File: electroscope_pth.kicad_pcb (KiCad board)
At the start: 2 copper layers, 17 parts, among them Q1 Q_PNP_EBC, Q2 Q_NPN_EBC, Q3 Q_PNP_EBC, Q4 Q_NPN_EBC, Q5 Q_PNP_EBC, Q6 Q_NPN_EBC, U1 ANT, U2 ANT

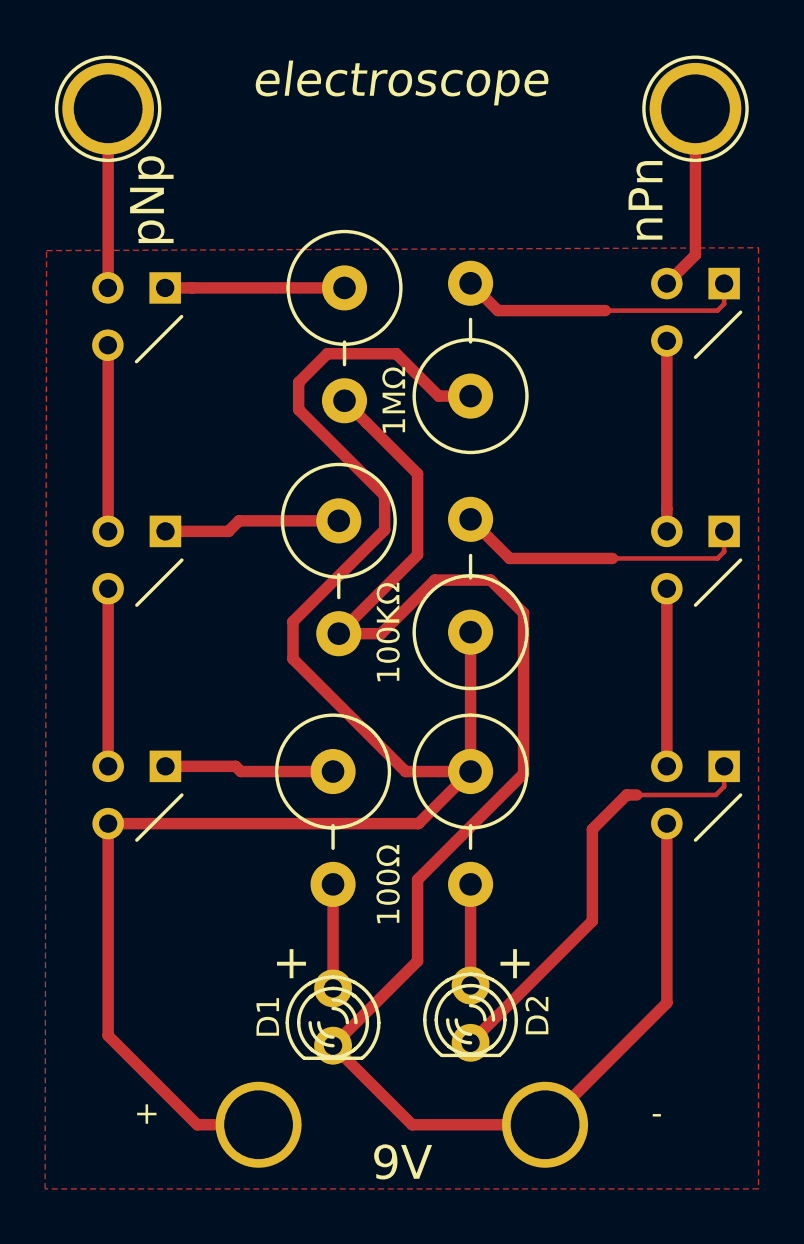
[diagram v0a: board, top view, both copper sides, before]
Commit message: Route to the edges of the board
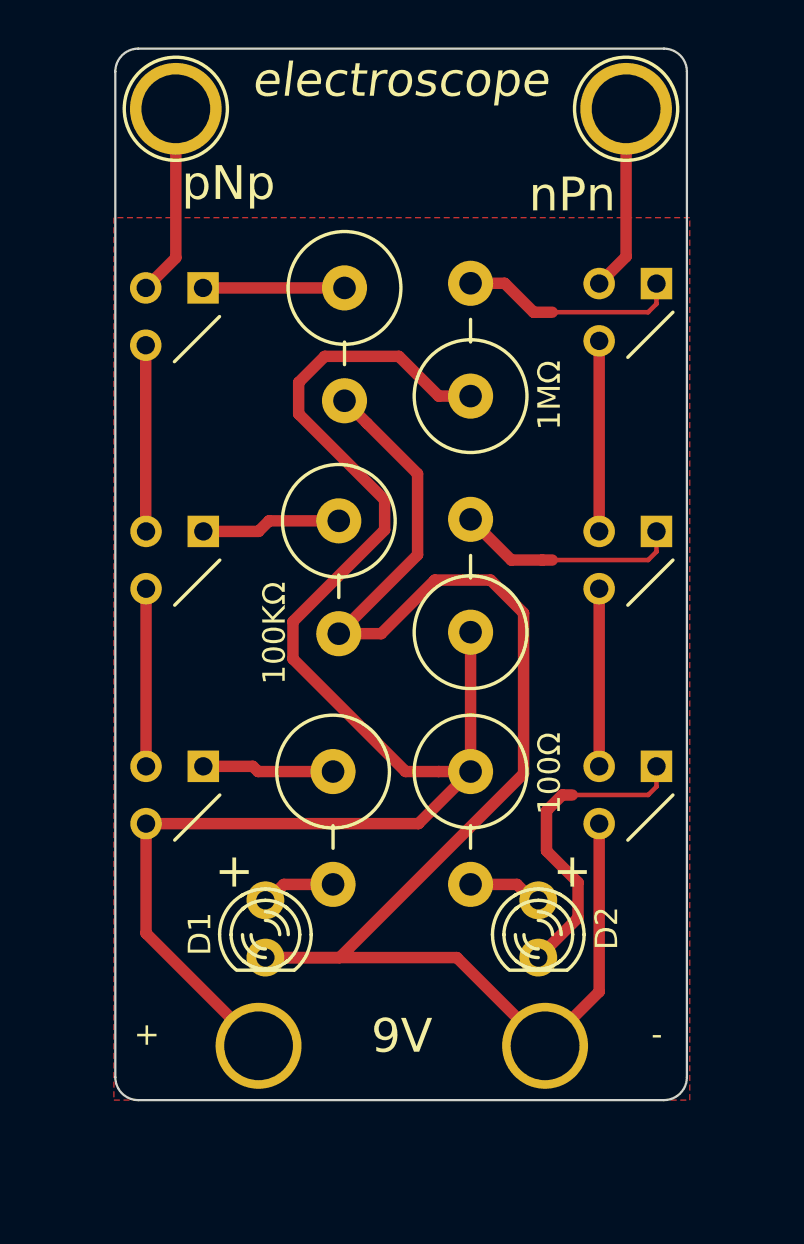
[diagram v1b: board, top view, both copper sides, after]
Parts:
- moved D1 4.92 mm to (133.7, 107.2)
- moved D2 4.82 mm to (145.8, 107.2)
- moved BT1 3.50 mm to (139.8, 112.5)
- moved U1 3.07 mm to (149.7, 70.9)
- moved U2 3.00 mm to (129.7, 70.9)
- moved Q2 3.00 mm to (149.8, 79.9)
- moved Q4 3.00 mm to (149.8, 90.9)
- moved Q6 3.00 mm to (149.8, 101.3)
- moved Q1 1.68 mm to (129.7, 101.3)
- moved Q3 1.68 mm to (129.7, 90.9)
- moved Q5 1.68 mm to (129.7, 80.1)
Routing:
- net VCC: track 75.3 -> 67.7 mm
- net Net-(D2-Pad2): track 19.2 -> 14.0 mm
- net Net-(Q2-Pad3): track 12.8 -> 9.83 mm
- net Net-(Q4-Pad3): track 13.0 -> 10.0 mm
- net GND: track 72.0 -> 69.7 mm
- net Net-(Q3-Pad3): track 7.88 -> 6.20 mm
- net Net-(Q1-Pad3): track 7.52 -> 5.85 mm
- net Net-(Q5-Pad3): track 7.95 -> 6.27 mm
- net Net-(D1-Pad1): track 4.61 -> 3.29 mm
- net Net-(D2-Pad1): track 4.48 -> 3.29 mm
- net Net-(Q5-Pad2): track 7.95 -> 8.49 mm
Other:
- board outline added: 25.3 x 46.6 mm

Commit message: More rounding and compaction
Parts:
- moved U1 2.06 mm to (147.7, 71.4)
- moved U2 2.06 mm to (131.7, 71.4)
- moved Q3 2.05 mm to (131.7, 90.4)
- moved Q1 2.01 mm to (131.7, 101.5)
- moved Q2 2.00 mm to (147.8, 79.9)
- moved Q4 2.00 mm to (147.8, 90.9)
- moved Q5 2.00 mm to (131.7, 80.1)
- moved Q6 2.00 mm to (147.8, 101.3)
- moved D1 1.22 mm to (132.7, 106.5)
- moved D2 1.22 mm to (146.8, 106.5)
- moved BT1 1.00 mm to (139.8, 111.5)
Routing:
- net GND: track 69.7 -> 57.6 mm
- net Net-(D2-Pad2): track 14.0 -> 8.70 mm
- net VCC: track 67.7 -> 63.8 mm
- net Net-(Q3-Pad3): track 6.20 -> 4.00 mm
- net Net-(Q1-Pad3): track 5.85 -> 3.75 mm
- net Net-(Q4-Pad3): track 10.0 -> 7.99 mm
- net Net-(Q5-Pad3): track 6.27 -> 4.27 mm
- net Net-(Q2-Pad3): track 9.83 -> 7.88 mm
- net Net-(D2-Pad1): track 3.29 -> 4.00 mm
- net Net-(D1-Pad1): track 3.29 -> 4.00 mm
- net Net-(Q1-Pad2): track 7.87 -> 8.57 mm
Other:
- board size 25.3 x 46.6 mm -> 21.3 x 45.7 mm
